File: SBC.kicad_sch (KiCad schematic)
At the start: 0 parts

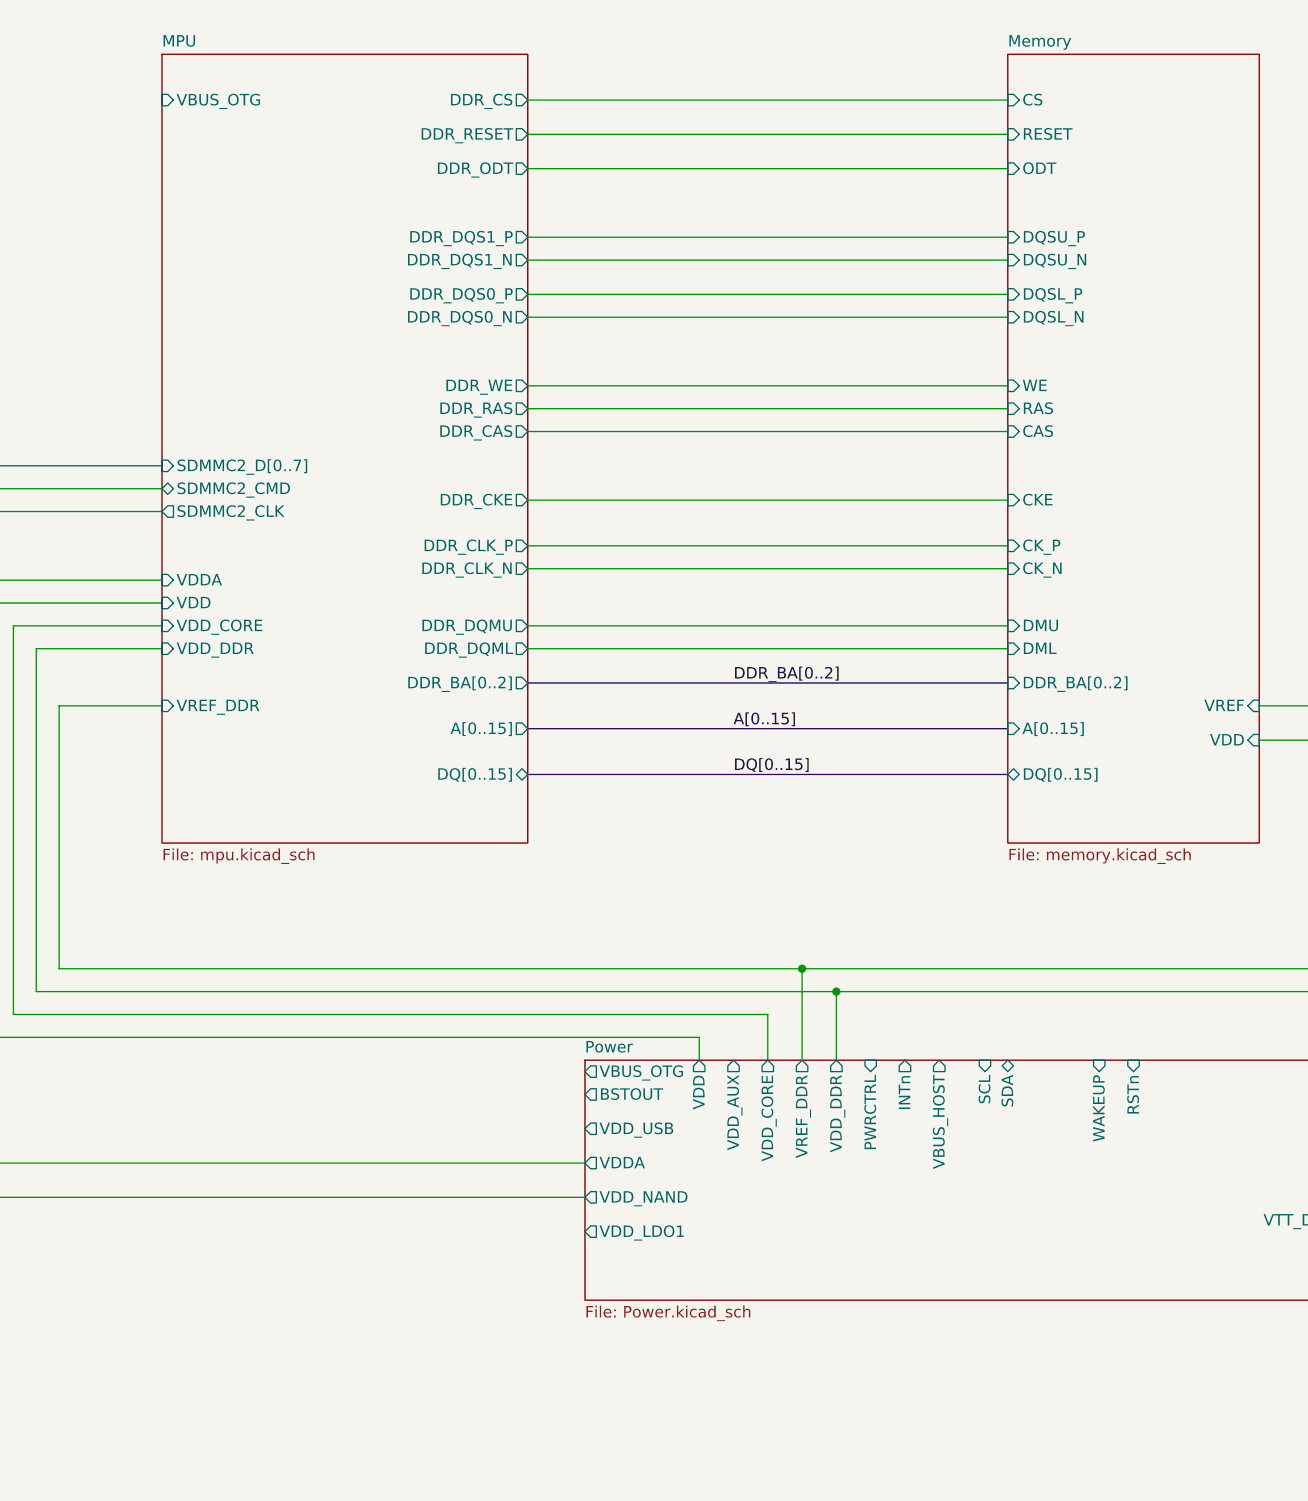
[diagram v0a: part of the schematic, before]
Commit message: Added USB, power and other signals
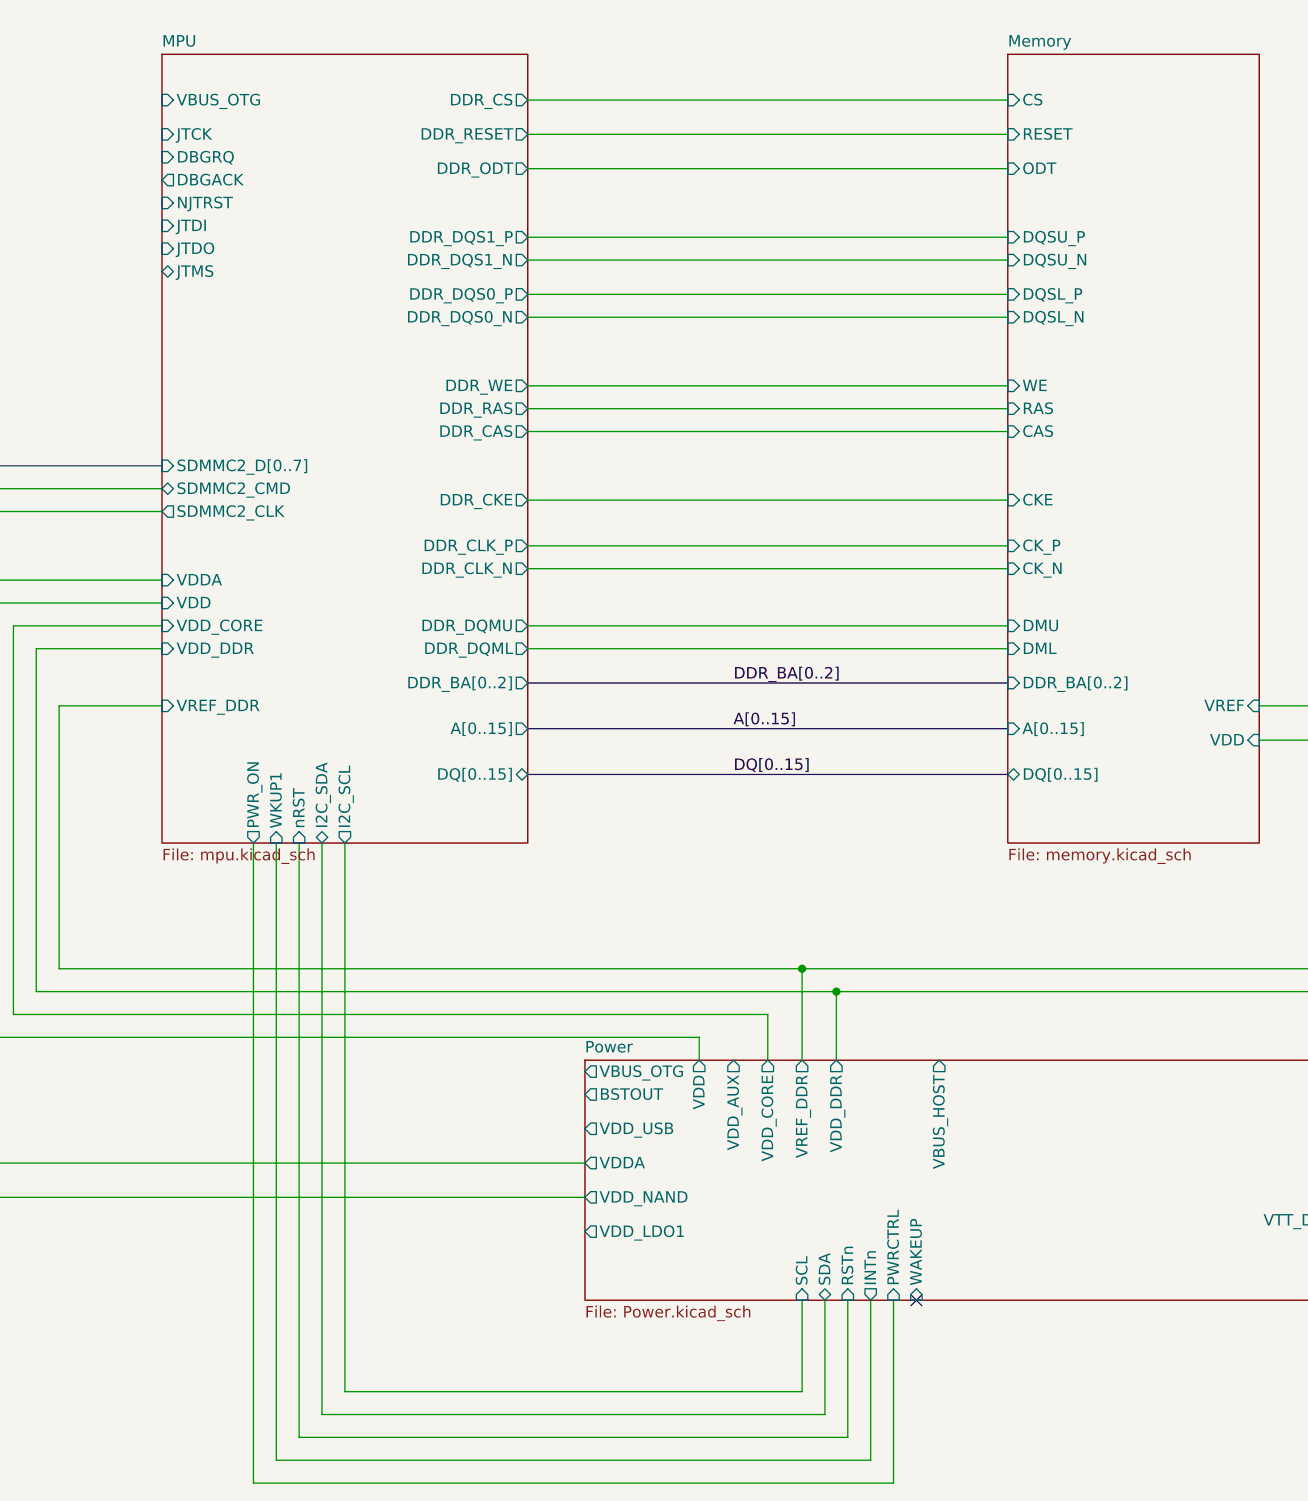
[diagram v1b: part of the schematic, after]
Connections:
- no-connect marks 0 -> 1
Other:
- sheet MPU ports: added DBGACK, DBGRQ, I2C_SCL, I2C_SDA, JTCK, JTDI, JTDO, JTMS, NJTRST, PWR_ON, WKUP1, nRST; removed none

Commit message: Working on Ethernet connections
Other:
- added sheet Ethernet (ethernet.kicad_sch)
- sheet MPU ports: added ETH1_MDC, ETH1_RMII_CRS_DV, ETH1_RMII_REF_CLK, ETH1_RMII_RXD0, ETH1_RMII_RXD1, ETH1_RMII_TXD0, ETH1_RMII_TXD1, ETH1_RMII_TX_EN, ETH_MDIO, ETH_PHY_INTn, ETH_RESETn, OTG_ID, USB_DM1, USB_DM2, USB_DP1, USB_DP2; removed none

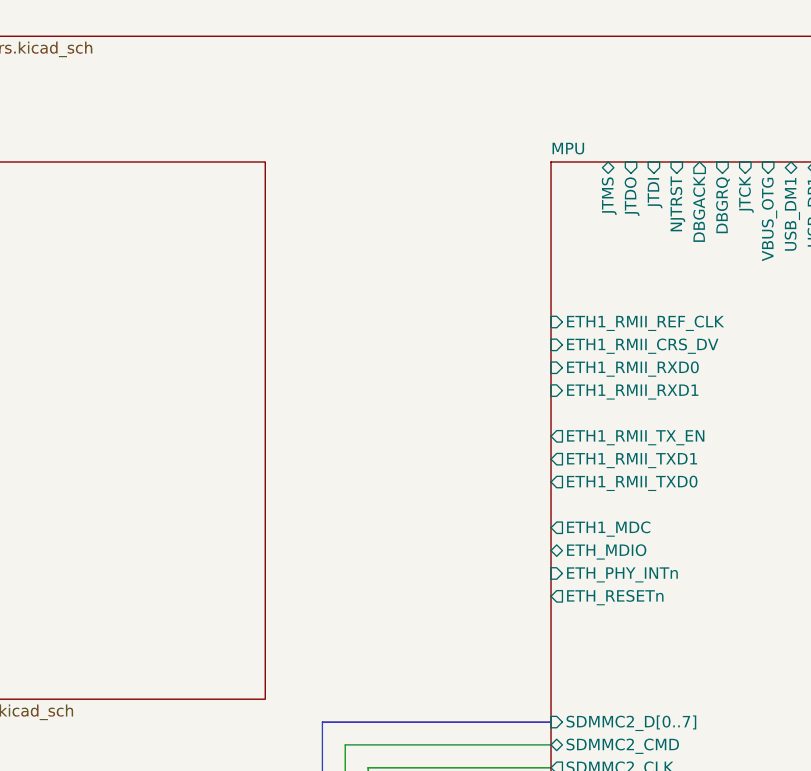
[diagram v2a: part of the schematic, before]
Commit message: Still updating ethernet phy
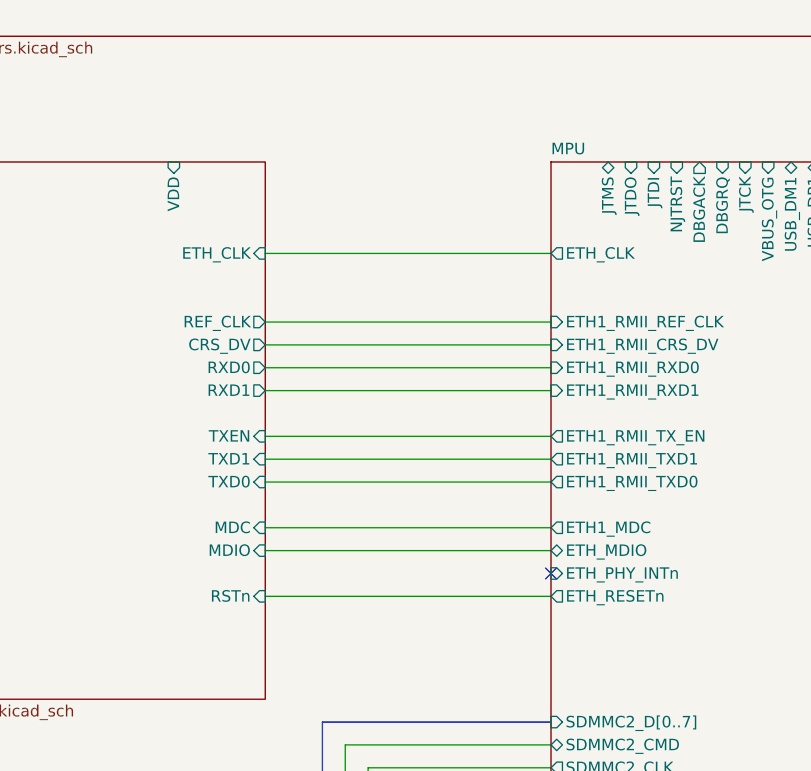
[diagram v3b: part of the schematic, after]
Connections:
- no-connect marks 1 -> 2
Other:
- sheet Ethernet ports: added CRS_DV, ETH_CLK, MDC, MDIO, REF_CLK, RSTn, RXD0, RXD1, TXD0, TXD1, TXEN, VDD; removed none
- sheet MPU ports: added ETH_CLK; removed none
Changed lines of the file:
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@@
 		(at 252.73 231.14)
 	)
+	(no_connect
+		(at 160.02 121.92)
+	)
 	(bus
 		(pts
@@
 	(wire
 		(pts
+			(xy 128.27 96.52) (xy 160.02 96.52)
+		)
+		(stroke
+			(width 0)
+			(type default)
+		)
+	)
+	(wire
+		(pts
 			(xy 186.69 243.84) (xy 242.57 243.84)
 		)
@@
 	(wire
 		(pts
+			(xy 128.27 106.68) (xy 160.02 106.68)
+		)
+		(stroke
+			(width 0)
+			(type default)
+		)
+	)
+	(wire
+		(pts
+			(xy 128.27 111.76) (xy 160.02 111.76)
+		)
+		(stroke
+			(width 0)
+			(type default)
+		)
+	)
+	(wire
+		(pts
 			(xy 290.83 165.1) (xy 304.8 165.1)
 		)
@@
 	(wire
 		(pts
+			(xy 128.27 93.98) (xy 160.02 93.98)
+		)
+		(stroke
+			(width 0)
+			(type default)
+		)
+	)
+	(wire
+		(pts
 			(xy 149.86 201.93) (xy 149.86 153.67)
 		)
@@
 	(wire
 		(pts
+			(xy 128.27 119.38) (xy 160.02 119.38)
+		)
+		(stroke
+			(width 0)
+			(type default)
+		)
+	)
+	(wire
+		(pts
 			(xy 209.55 105.41) (xy 262.89 105.41)
 		)
@@
 		)
 	)
+	(wire
+		(pts
+			(xy 128.27 101.6) (xy 160.02 101.6)
+		)
+		(stroke
+			(width 0)
+			(type default)
+		)
+	)
+	(wire
+		(pts
+			(xy 128.27 116.84) (xy 160.02 116.84)
+		)
+		(stroke
+			(width 0)
+			(type default)
+		)
+	)
+	(wire
+		(pts
+			(xy 128.27 99.06) (xy 160.02 99.06)
+		)
+		(stroke
+			(width 0)
+			(type default)
+		)
+	)
 	(bus
 		(pts
@@
 	(wire
 		(pts
+			(xy 128.27 124.46) (xy 160.02 124.46)
+		)
+		(stroke
+			(width 0)
+			(type default)
+		)
+	)
+	(wire
+		(pts
 			(xy 240.03 194.31) (xy 157.48 194.31)
 		)
@@
 	(wire
 		(pts
+			(xy 128.27 86.36) (xy 160.02 86.36)
+		)
+		(stroke
+			(width 0)
+			(type default)
+		)
+	)
+	(wire
+		(pts
 			(xy 304.8 165.1) (xy 304.8 196.85)
 		)
@@
 		(pts
 			(xy 152.4 156.21) (xy 160.02 156.21)
+		)
+		(stroke
+			(width 0)
+			(type default)
+		)
+	)
+	(wire
+		(pts
+			(xy 128.27 109.22) (xy 160.02 109.22)
 		)
 		(stroke
@@
 			)
 		)
+		(pin "ETH_CLK" output
+			(at 160.02 86.36 180)
+			(effects
+				(font
+					(size 1.27 1.27)
+				)
+				(justify left)
+			)
+		)
 		(instances
 			(project "SBC"
@@
 			)
 		)
+		(pin "TXD0" input
+			(at 128.27 111.76 0)
+			(effects
+				(font
+					(size 1.27 1.27)
+				)
+				(justify right)
+			)
+		)
+		(pin "RXD1" output
+			(at 128.27 101.6 0)
+			(effects
+				(font
+					(size 1.27 1.27)
+				)
+				(justify right)
+			)
+		)
+		(pin "TXD1" input
+			(at 128.27 109.22 0)
+			(effects
+				(font
+					(size 1.27 1.27)
+				)
+				(justify right)
+			)
+		)
+		(pin "RXD0" output
+			(at 128.27 99.06 0)
+			(effects
+				(font
+					(size 1.27 1.27)
+				)
+				(justify right)
+			)
+		)
+		(pin "TXEN" input
+			(at 128.27 106.68 0)
+			(effects
+				(font
+					(size 1.27 1.27)
+				)
+				(justify right)
+			)
+		)
+		(pin "VDD" input
+			(at 118.11 76.2 90)
+			(effects
+				(font
+					(size 1.27 1.27)
+				)
+				(justify right)
+			)
+		)
+		(pin "ETH_CLK" input
+			(at 128.27 86.36 0)
+			(effects
+				(font
+					(size 1.27 1.27)
+				)
+				(justify right)
+			)
+		)
+		(pin "MDC" input
+			(at 128.27 116.84 0)
+			(effects
+				(font
+					(size 1.27 1.27)
+				)
+				(justify right)
+			)
+		)
+		(pin "MDIO" input
+			(at 128.27 119.38 0)
+			(effects
+				(font
+					(size 1.27 1.27)
+				)
+				(justify right)
+			)
+		)
+		(pin "CRS_DV" output
+			(at 128.27 96.52 0)
+			(effects
+				(font
+					(size 1.27 1.27)
+				)
+				(justify right)
+			)
+		)
+		(pin "RSTn" input
+			(at 128.27 124.46 0)
+			(effects
+				(font
+					(size 1.27 1.27)
+				)
+				(justify right)
+			)
+		)
+		(pin "REF_CLK" output
+			(at 128.27 93.98 0)
+			(effects
+				(font
+					(size 1.27 1.27)
+				)
+				(justify right)
+			)
+		)
